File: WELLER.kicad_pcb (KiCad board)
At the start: 2 copper layers, 20 x 100 mm, 74 parts, among them J1 Jack-DC, J2 AudioJack3_Ground_SwitchR, J3 debug+programing, J4 I2c oled, Q1 DMP2018LFK, SW1 SW_Push_SPDT, SW2 SW_Push, SW3 SW_Push, U1 AP1117-33, U2 LTC4440IS6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

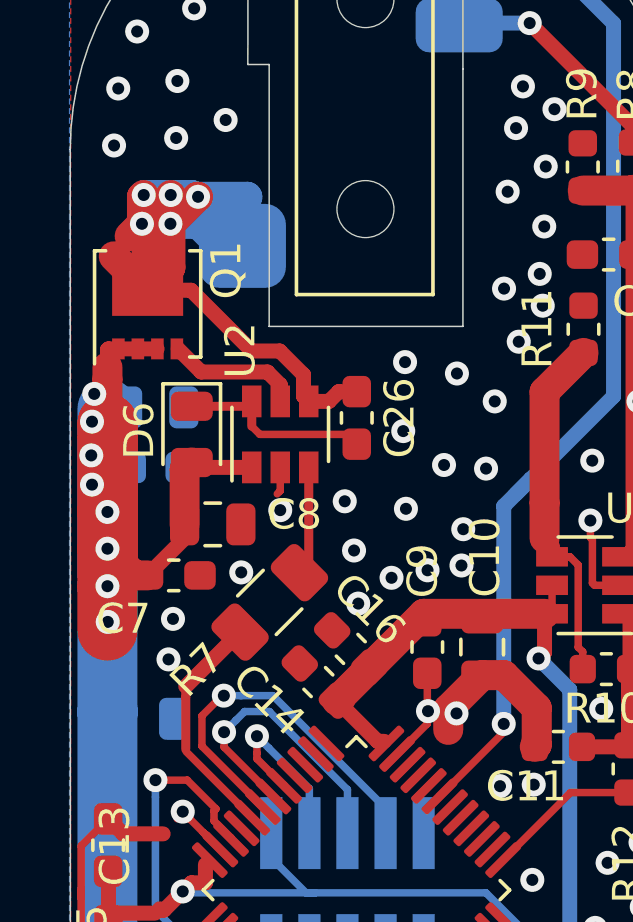
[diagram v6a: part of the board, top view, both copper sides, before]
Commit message: zmiana tranzystora
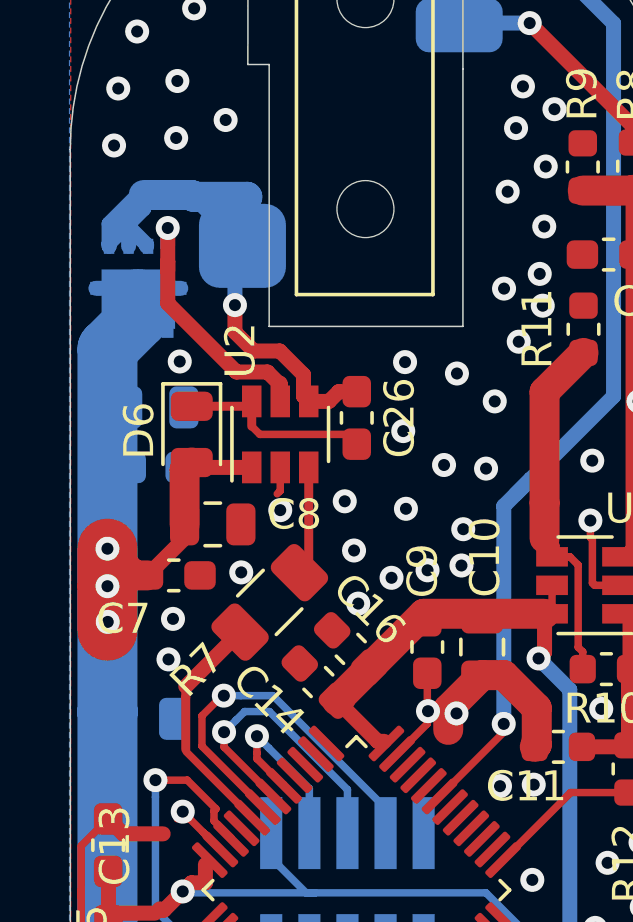
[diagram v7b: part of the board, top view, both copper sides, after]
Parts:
- Q1: value DMP2018LFK -> AON7403; footprint Package_SON:Diodes_PowerDI3333-8 -> symbols:DFN_3X3_EP; moved to B.Cu
- moved Q1 0.61 mm to (122.3, 39.6), turned to 0 degrees
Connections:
- Q1 pad 1: /tip_driving/12V -> /tip_driving/heater
- Q1 pad 2: /tip_driving/12V -> /tip_driving/heater
- Q1 pad 3: /tip_driving/12V -> /tip_driving/heater
- Q1 pad 5: /tip_driving/heater -> /tip_driving/12V
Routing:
- net /tip_driving/12V: track 131.1 -> 124.6 mm, vias 17 -> 12
- net Net-(Q1-Pad4): track 4.45 -> 9.46 mm, vias 0 -> 1
- net /tip_driving/heater: track 26.4 -> 23.1 mm, vias 5 -> 1
- net GND: vias 105 -> 106

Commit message: update front endu do termopary i przełącznika zasilającego
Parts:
- added C33: 10n, Capacitor_SMD:C_0603_1608Metric_Pad1.05x0.95mm_HandSolder, F.Cu at (137.7, 40.4)
- added C34: 100n, Capacitor_SMD:C_0603_1608Metric_Pad1.05x0.95mm_HandSolder, F.Cu at (136.4, 36.1)
- added C35: 100n, Capacitor_SMD:C_0603_1608Metric_Pad1.05x0.95mm_HandSolder, F.Cu at (138.3, 52.4)
- added D7: D_Zener, Diode_SMD:D_0805_2012Metric_Castellated, F.Cu at (124.8, 109.4)
- added Q2: AON7403, symbols:DFN_3X3_EP, F.Cu at (128.2, 105.7)
- added Q3: AON7403, symbols:DFN_3X3_EP, F.Cu at (123.2, 105.7)
- added R18: 10meg, Resistor_SMD:R_0603_1608Metric, F.Cu at (131.3, 42.5)
- added R19: 1meg, Resistor_SMD:R_0603_1608Metric, F.Cu at (137.6, 44.8)
- added R25: 10meg, Resistor_SMD:R_0603_1608Metric, F.Cu at (132.7, 49.1)
- added R26: 100k, Resistor_SMD:R_0603_1608Metric, F.Cu at (138.3, 49.2)
- added R27: 150, Resistor_SMD:R_0603_1608Metric, F.Cu at (131.2, 45.6)
- added R28: 68, Resistor_SMD:R_0603_1608Metric, F.Cu at (129.7, 47.2)
- C11: value n.c. -> 100n
- C6: value 100n -> 10n
- R11: value 270 -> 1k
- R9: value 1meg -> 100k
- U3: value MCP603-xCH -> MCP6N16; footprint TO_SOT_Packages_SMD:SOT-23-6 -> Package_SO:MSOP-8_3x3mm_P0.65mm
- moved R9 68.9 mm to (131.6, 104.3), turned to 0 degrees
- moved R10 54.8 mm to (131.6, 106.7), turned to 0 degrees
- moved C1 8.59 mm to (122.7, 96.2), turned to 0 degrees
- moved C2 8.56 mm to (122.2, 100.0), turned to 0 degrees
- moved C3 8.51 mm to (122.1, 98.2), turned to 0 degrees
- moved U3 5.26 mm to (134.9, 44.8), turned to 270 degrees
- moved R11 2.29 mm to (135.2, 39.7), turned to 270 degrees
- moved C6 0.23 mm to (137.7, 38.6), turned to 0 degrees
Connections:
- C11 pad 1: Net-(C11-Pad1) -> /stm32/termocouple
- C6 pad 1: Net-(C6-Pad1) -> Net-(C34-Pad1)
- J3 pad 6: Net-(J3-Pad6) -> (no net)
- J3 pad 8: Net-(J3-Pad8) -> (no net)
- R10 pad 1: Net-(C11-Pad1) -> Net-(D7-Pad2)
- R11 pad 1: Net-(R10-Pad2) -> GND
- R11 pad 2: GND -> Net-(C33-Pad2)
- R12 pad 2: Net-(C11-Pad1) -> Net-(C35-Pad1)
- R8 pad 2: Net-(C6-Pad1) -> Net-(C34-Pad1)
- R9 pad 1: Net-(C6-Pad1) -> Net-(D7-Pad1)
- R9 pad 2: GND -> Net-(R10-Pad2)
- SW1 pad 1: Net-(J1-Pad1) -> (no net)
- SW1 pad 2: /tip_driving/12V -> Net-(R10-Pad2)
- SW1 pad 3: /tip_driving/12V -> GND
- U3 pad 1: Net-(C11-Pad1) -> Net-(R19-Pad1)
- U3 pad 2: GND -> Net-(C33-Pad2)
- U3 pad 3: Net-(C6-Pad1) -> Net-(C34-Pad1)
- U3 pad 4: Net-(R10-Pad2) -> GND
- U3 pad 5: /tip_driving/3.3V_analog -> Net-(R25-Pad1)
- U3 pad 6: /tip_driving/3.3V_analog -> Net-(C35-Pad2)
- U4 pad 12: Net-(U4-Pad12) -> (no net)
- U4 pad 14: Net-(U4-Pad14) -> (no net)
- U4 pad 15: Net-(U4-Pad15) -> (no net)
- U4 pad 16: Net-(U4-Pad16) -> (no net)
- U4 pad 17: Net-(U4-Pad17) -> (no net)
- U4 pad 18: Net-(U4-Pad18) -> (no net)
- U4 pad 20: Net-(U4-Pad20) -> (no net)
- U4 pad 21: Net-(U4-Pad21) -> (no net)
- U4 pad 22: Net-(U4-Pad22) -> (no net)
- U4 pad 25: Net-(U4-Pad25) -> (no net)
- U4 pad 26: Net-(U4-Pad26) -> (no net)
- U4 pad 27: Net-(U4-Pad27) -> (no net)
- U4 pad 28: Net-(U4-Pad28) -> (no net)
- U4 pad 33: Net-(U4-Pad33) -> (no net)
- U4 pad 38: Net-(U4-Pad38) -> (no net)
- U4 pad 4: Net-(U4-Pad4) -> (no net)
- U4 pad 45: Net-(U4-Pad45) -> (no net)
- U4 pad 46: Net-(U4-Pad46) -> (no net)
- U4 pad 5: Net-(U4-Pad5) -> (no net)
- U4 pad 6: Net-(U4-Pad6) -> (no net)
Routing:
- net Net-(D7-Pad1): track 0.00 -> 30.7 mm
- net /tip_driving/12V: track 124.6 -> 149.9 mm
- net Net-(C34-Pad1): track 0.00 -> 24.4 mm
- net Net-(D7-Pad2): track 0.00 -> 16.5 mm, vias 0 -> 3
- net /tip_driving/3.3V_analog: track 152.6 -> 167.6 mm, vias 33 -> 34
- net Net-(C6-Pad1): track 14.0 -> 0.00 mm, vias 1 -> 0
- net Net-(C35-Pad1): track 0.00 -> 13.7 mm
- net Net-(C35-Pad2): track 0.00 -> 13.2 mm
- net Net-(C33-Pad2): track 0.00 -> 11.1 mm
- net Net-(C11-Pad1): track 6.04 -> 0.00 mm
- net Net-(R19-Pad1): track 0.00 -> 2.39 mm
- net Net-(R25-Pad1): track 0.00 -> 2.29 mm
- net Net-(J1-Pad1): track 10.3 -> 8.60 mm
- net Net-(R10-Pad2): track 12.2 -> 10.5 mm
- net /stm32/termocouple: track 5.11 -> 6.79 mm
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- removed copper zone on F.Cu, net /tip_driving/12V
